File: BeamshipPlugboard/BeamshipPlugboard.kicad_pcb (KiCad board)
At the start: 2 copper layers, 150.2 x 27.9 mm, 4 parts, among them J1 BEAMSPRING PLUGBOARD COLUMNS, J2 BEAMSPRING PLUGBOARD ROWS, J7 Conn_01x34

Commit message: Added some notes to beamspring plugboard
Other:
- board text added: "The left side must also be cut off, because the beamship uses 2x30 pin connectors, and this pluboard doesn't have the full width. (Note: there are two dummy pins in-between)"
- board text added: "The right side of modern connectors must be cut of in order to not interfere with the mounting plate."
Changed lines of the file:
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@@
   (general
     (thickness 1.6)
-    (drawings 33)
+    (drawings 35)
     (tracks 615)
     (zones 0)
@@
       (effects (font (size 1 1) (thickness 0.15)))
     )
+    (fp_circle (center 0 0) (end 1.6 0) (layer F.CrtYd) (width 0.05))
+    (fp_circle (center 0 0) (end 2.2 0) (layer Cmts.User) (width 0.15))
     (fp_circle (center 0 0) (end 2 0) (layer F.SilkS) (width 0.3))
-    (fp_circle (center 0 0) (end 2.2 0) (layer Cmts.User) (width 0.15))
-    (fp_circle (center 0 0) (end 1.6 0) (layer F.CrtYd) (width 0.05))
     (fp_text user "CHASSIS GND" (at 0.5792 3.8098 180 unlocked) (layer F.SilkS)
       (effects (font (size 1 1) (thickness 0.15)))
@@
       (effects (font (size 1 1) (thickness 0.15)))
     )
+    (fp_line (start -58.8 -9.2) (end -58.8 0.6) (layer F.CrtYd) (width 0.05))
+    (fp_line (start -58.8 0.6) (end 74.64 0.6) (layer F.CrtYd) (width 0.05))
+    (fp_line (start 74.64 0.6) (end 74.64 -9.2) (layer F.CrtYd) (width 0.05))
     (fp_line (start 74.64 -9.2) (end -58.8 -9.2) (layer F.CrtYd) (width 0.05))
-    (fp_line (start 74.64 0.6) (end 74.64 -9.2) (layer F.CrtYd) (width 0.05))
-    (fp_line (start -58.8 0.6) (end 74.64 0.6) (layer F.CrtYd) (width 0.05))
-    (fp_line (start -58.8 -9.2) (end -58.8 0.6) (layer F.CrtYd) (width 0.05))
     (pad 34 thru_hole oval (at 73.26 -7.53) (size 3.45 1.55) (drill oval 2.7 0.8) (layers *.Cu *.Mask)
       (net 32 /BSSENSE8))
@@
     (descr "Through hole straight socket strip, 1x27, 2.54mm pitch, single row (from Kicad 4.0.7), script generated")
     (tags "Through hole socket strip THT 1x27 2.54mm single row")
-    (fp_text reference J1 (at 0 2.77 90) (layer B.SilkS)
+    (fp_text reference J1 (at 0 2.77 90) (layer B.SilkS) hide
       (effects (font (size 1 1) (thickness 0.15)) (justify mirror))
     )
@@
       (effects (font (size 1 1) (thickness 0.15)) (justify mirror))
     )
+    (fp_line (start -1.27 1.27) (end 0.635 1.27) (layer B.Fab) (width 0.1))
+    (fp_line (start 0.635 1.27) (end 1.27 0.635) (layer B.Fab) (width 0.1))
+    (fp_line (start 1.27 0.635) (end 1.27 -67.31) (layer B.Fab) (width 0.1))
+    (fp_line (start 1.27 -67.31) (end -1.27 -67.31) (layer B.Fab) (width 0.1))
+    (fp_line (start -1.27 -67.31) (end -1.27 1.27) (layer B.Fab) (width 0.1))
+    (fp_line (start -1.33 -1.27) (end 1.33 -1.27) (layer B.SilkS) (width 0.12))
+    (fp_line (start -1.33 -1.27) (end -1.33 -67.37) (layer B.SilkS) (width 0.12))
+    (fp_line (start -1.33 -67.37) (end 1.33 -67.37) (layer B.SilkS) (width 0.12))
+    (fp_line (start 1.33 -1.27) (end 1.33 -67.37) (layer B.SilkS) (width 0.12))
+    (fp_line (start 1.33 1.33) (end 1.33 0) (layer B.SilkS) (width 0.12))
+    (fp_line (start 0 1.33) (end 1.33 1.33) (layer B.SilkS) (width 0.12))
+    (fp_line (start -1.8 1.8) (end 1.75 1.8) (layer B.CrtYd) (width 0.05))
+    (fp_line (start 1.75 1.8) (end 1.75 -67.8) (layer B.CrtYd) (width 0.05))
+    (fp_line (start 1.75 -67.8) (end -1.8 -67.8) (layer B.CrtYd) (width 0.05))
     (fp_line (start -1.8 -67.8) (end -1.8 1.8) (layer B.CrtYd) (width 0.05))
-    (fp_line (start 1.75 -67.8) (end -1.8 -67.8) (layer B.CrtYd) (width 0.05))
-    (fp_line (start 1.75 1.8) (end 1.75 -67.8) (layer B.CrtYd) (width 0.05))
-    (fp_line (start -1.8 1.8) (end 1.75 1.8) (layer B.CrtYd) (width 0.05))
-    (fp_line (start 0 1.33) (end 1.33 1.33) (layer B.SilkS) (width 0.12))
-    (fp_line (start 1.33 1.33) (end 1.33 0) (layer B.SilkS) (width 0.12))
-    (fp_line (start 1.33 -1.27) (end 1.33 -67.37) (layer B.SilkS) (width 0.12))
-    (fp_line (start -1.33 -67.37) (end 1.33 -67.37) (layer B.SilkS) (width 0.12))
-    (fp_line (start -1.33 -1.27) (end -1.33 -67.37) (layer B.SilkS) (width 0.12))
-    (fp_line (start -1.33 -1.27) (end 1.33 -1.27) (layer B.SilkS) (width 0.12))
-    (fp_line (start -1.27 -67.31) (end -1.27 1.27) (layer B.Fab) (width 0.1))
-    (fp_line (start 1.27 -67.31) (end -1.27 -67.31) (layer B.Fab) (width 0.1))
-    (fp_line (start 1.27 0.635) (end 1.27 -67.31) (layer B.Fab) (width 0.1))
-    (fp_line (start 0.635 1.27) (end 1.27 0.635) (layer B.Fab) (width 0.1))
-    (fp_line (start -1.27 1.27) (end 0.635 1.27) (layer B.Fab) (width 0.1))
     (fp_text user %R (at 0 -33.02 180) (layer B.Fab)
       (effects (font (size 1 1) (thickness 0.15)) (justify mirror))
@@
     (descr "Through hole straight socket strip, 1x12, 2.54mm pitch, single row (from Kicad 4.0.7), script generated")
     (tags "Through hole socket strip THT 1x12 2.54mm single row")
-    (fp_text reference J2 (at 0 2.77 -90) (layer B.SilkS)
+    (fp_text reference J2 (at 0 2.77 -90) (layer B.SilkS) hide
       (effects (font (size 1 1) (thickness 0.15)) (justify mirror))
     )
@@
       (effects (font (size 1 1) (thickness 0.15)) (justify mirror))
     )
+    (fp_line (start -1.27 1.27) (end 0.635 1.27) (layer B.Fab) (width 0.1))
+    (fp_line (start 0.635 1.27) (end 1.27 0.635) (layer B.Fab) (width 0.1))
+    (fp_line (start 1.27 0.635) (end 1.27 -29.21) (layer B.Fab) (width 0.1))
+    (fp_line (start 1.27 -29.21) (end -1.27 -29.21) (layer B.Fab) (width 0.1))
+    (fp_line (start -1.27 -29.21) (end -1.27 1.27) (layer B.Fab) (width 0.1))
+    (fp_line (start -1.33 -1.27) (end 1.33 -1.27) (layer B.SilkS) (width 0.12))
+    (fp_line (start -1.33 -1.27) (end -1.33 -29.27) (layer B.SilkS) (width 0.12))
+    (fp_line (start -1.33 -29.27) (end 1.33 -29.27) (layer B.SilkS) (width 0.12))
+    (fp_line (start 1.33 -1.27) (end 1.33 -29.27) (layer B.SilkS) (width 0.12))
+    (fp_line (start 1.33 1.33) (end 1.33 0) (layer B.SilkS) (width 0.12))
+    (fp_line (start 0 1.33) (end 1.33 1.33) (layer B.SilkS) (width 0.12))
+    (fp_line (start -1.8 1.8) (end 1.75 1.8) (layer B.CrtYd) (width 0.05))
+    (fp_line (start 1.75 1.8) (end 1.75 -29.7) (layer B.CrtYd) (width 0.05))
+    (fp_line (start 1.75 -29.7) (end -1.8 -29.7) (layer B.CrtYd) (width 0.05))
     (fp_line (start -1.8 -29.7) (end -1.8 1.8) (layer B.CrtYd) (width 0.05))
-    (fp_line (start 1.75 -29.7) (end -1.8 -29.7) (layer B.CrtYd) (width 0.05))
-    (fp_line (start 1.75 1.8) (end 1.75 -29.7) (layer B.CrtYd) (width 0.05))
-    (fp_line (start -1.8 1.8) (end 1.75 1.8) (layer B.CrtYd) (width 0.05))
-    (fp_line (start 0 1.33) (end 1.33 1.33) (layer B.SilkS) (width 0.12))
-    (fp_line (start 1.33 1.33) (end 1.33 0) (layer B.SilkS) (width 0.12))
-    (fp_line (start 1.33 -1.27) (end 1.33 -29.27) (layer B.SilkS) (width 0.12))
-    (fp_line (start -1.33 -29.27) (end 1.33 -29.27) (layer B.SilkS) (width 0.12))
-    (fp_line (start -1.33 -1.27) (end -1.33 -29.27) (layer B.SilkS) (width 0.12))
-    (fp_line (start -1.33 -1.27) (end 1.33 -1.27) (layer B.SilkS) (width 0.12))
-    (fp_line (start -1.27 -29.21) (end -1.27 1.27) (layer B.Fab) (width 0.1))
-    (fp_line (start 1.27 -29.21) (end -1.27 -29.21) (layer B.Fab) (width 0.1))
-    (fp_line (start 1.27 0.635) (end 1.27 -29.21) (layer B.Fab) (width 0.1))
-    (fp_line (start 0.635 1.27) (end 1.27 0.635) (layer B.Fab) (width 0.1))
-    (fp_line (start -1.27 1.27) (end 0.635 1.27) (layer B.Fab) (width 0.1))
     (fp_text user %R (at 0 -13.97) (layer B.Fab)
       (effects (font (size 1 1) (thickness 0.15)) (justify mirror))
@@
     )
   )
+  (gr_text "The left side must also be cut off, because the beamship uses 2x30 pin connectors, and this pluboard doesn't have the full width. (Note: there are two dummy pins in-between)" (at 157.75 109.78 180) (layer B.SilkS)
+    (effects (font (size 1 1) (thickness 0.15)) (justify mirror))
+  )
+  (gr_text "The right side of modern connectors must be cut of in order to not interfere with the mounting plate." (at 128.43 112.17 180) (layer B.SilkS)
+    (effects (font (size 1 1) (thickness 0.15)) (justify mirror))
+  )
   (gr_text "Mount connectors on this side!" (at 177.7 116.8 180) (layer B.SilkS)
     (effects (font (size 1 1) (thickness 0.15)) (justify mirror))
@@
     (effects (font (size 1 1) (thickness 0.15)) (justify mirror))
   )
-  (gr_text "BEAMSHIP PLUGBOARD" (at 126.6 111.4 180) (layer B.SilkS)
+  (gr_text "BEAMSHIP PLUGBOARD" (at 174.94 119.3 180) (layer B.SilkS)
     (effects (font (size 1 1) (thickness 0.15)) (justify mirror))
   )

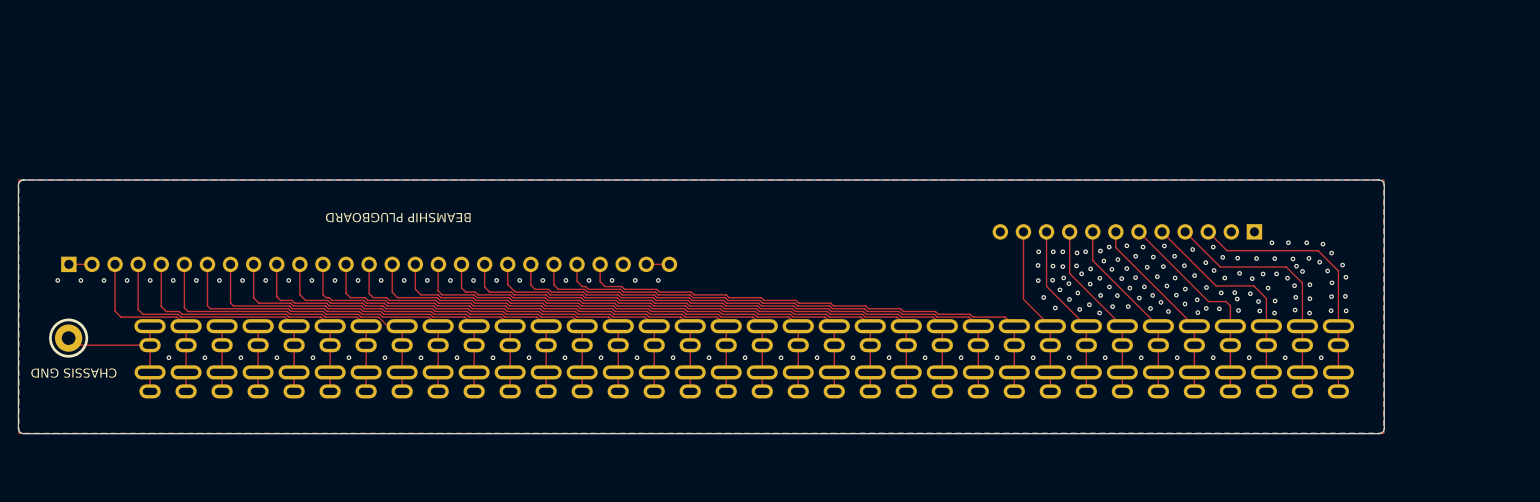
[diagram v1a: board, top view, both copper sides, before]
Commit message: Various changes to revision 0.1.1
General:
    Made mounting hole bigger (M3). And moved it a little bit so it doesn't interfere with some components.
    Star ground turned into single ground.
    Ground fills added everywhere.
    Many stitching vias added everywhere.
    Added JLCJLCJLCJLC magic string under pro micro. When ordering from JLCPCB, you can select for Order Number: "Specify Location"
    Bumped version number to 0.1.1
    Added silkscreen to mark rows/columns everywhere.
    Added optional holes for soldering grounding wires everywhere.
Controller:
    Added silkscreen to ease debugging, by marking various important nets.
    Rearranged some traces to maintain better separation between traces, and better ground reference.
Model F plugboard:
    Modified 3.96mm pitch holes, to hole sizes and pad sizes that match original xwhatsit model F controller
    Moved 3.96mm pitch holes closer to the edge, so it doesn't interfere with case in F AT cases.
    Added mounting holes
    Added holes to support 3178 keyboards.
Displaywriter:
    Addes support for more connector types. (The displaywriter daughterboard is now taller)
Beamspring:
    Bugfix to a mistake that only affected people that ran update footprints from library.
Beamship daughterboard:
    Added support for more connectors. Added breakoff-able mounting hole.
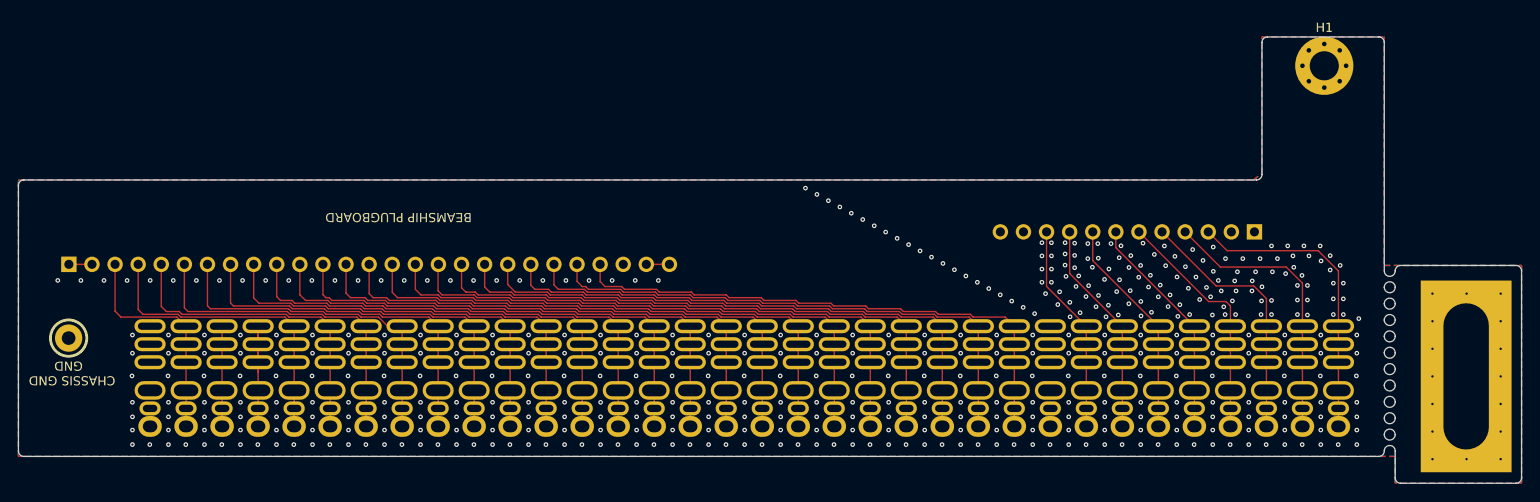
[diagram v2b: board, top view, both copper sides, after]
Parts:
- added H1: Grounded hole for M3 standoff, MountingHole:MountingHole_3.2mm_M3_Pad_Via, F.Cu at (228.3, 94.8)
- added H2: BEAMSHIP MOUNTING HOLE, TH-XWhatsIt:beamship_mounting_hole, F.Cu at (243.9, 129.0)
- J7: footprint TH-XWhatsIt:beamship_new -> TH-XWhatsIt:beamship_new_2
- moved J7 1.98 mm to (156.6, 133.0)
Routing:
- net /BSGROUND: track 40.3 -> 6.22 mm, vias 174 -> 468
- net Net-(J7-Pad4): track 7.17 -> 16.1 mm
- net /BSCOL3: track 31.3 -> 35.1 mm
- net Net-(J7-Pad3): track 7.17 -> 11.0 mm
- net /BSSENSE7: track 27.1 -> 31.0 mm
- net /BSSENSE6: track 24.7 -> 28.6 mm
- net /BSSENSE5: track 22.8 -> 26.7 mm
- net /BSSENSE4: track 21.1 -> 25.0 mm
- net /BSSENSE3: track 20.5 -> 24.4 mm
- net /BSSENSE2: track 19.9 -> 23.8 mm
- net /BSSENSE1: track 19.4 -> 23.2 mm
- net /BSCOL9: track 39.0 -> 42.9 mm
- net /BSCOL8: track 37.7 -> 41.6 mm
- net /BSCOL7: track 36.4 -> 40.2 mm
- net /BSCOL6: track 35.3 -> 39.2 mm
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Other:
- board size 150.2 x 27.9 mm -> 165.3 x 49.1 mm
- board text added: "Break off if not needed"
- board text added: "The right side of modern connectors must be cut off in order to not interfere with the mounting plate."
- board text removed: "The right side of modern connectors must be cut of in order to not interfere with the mounting plate."
